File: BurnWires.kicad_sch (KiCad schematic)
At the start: 29 parts, among them Q13 IRLML2803, Q14 SiRA99DP, Q15 IRFTS9342PBF, Q17 IRFTS9342PBF, Q19 IRFTS9342PBF

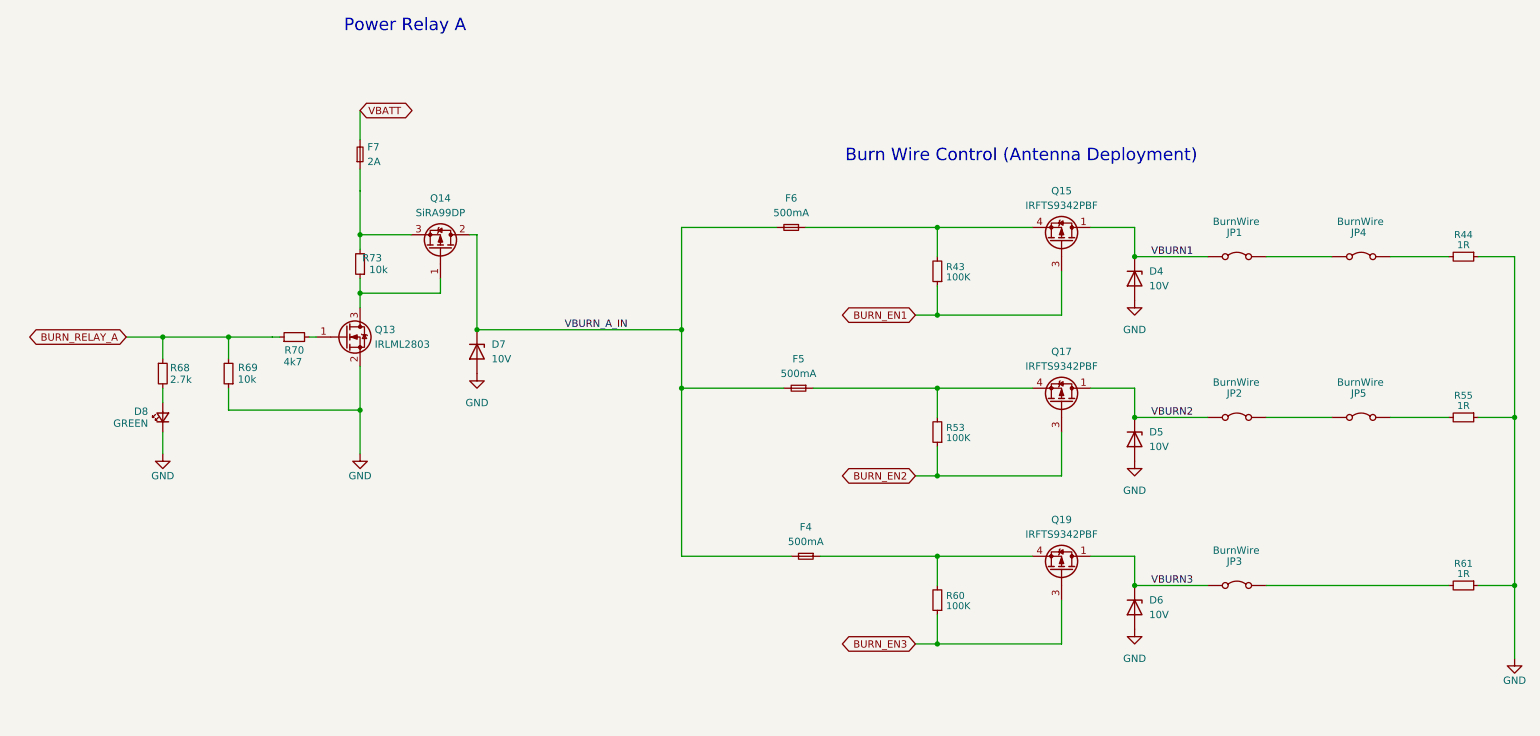
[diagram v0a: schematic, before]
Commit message: Updated burnwire footprint and fuse specs
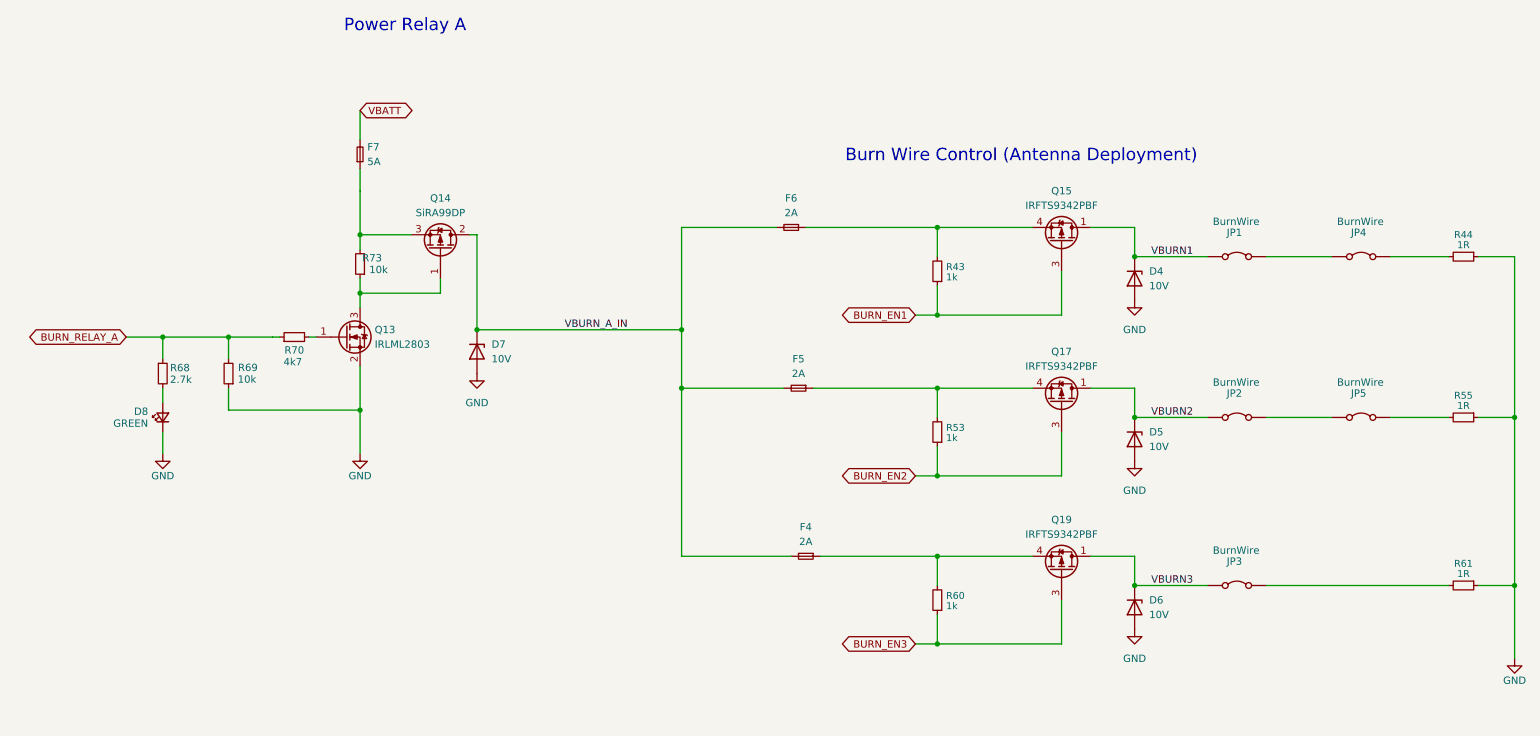
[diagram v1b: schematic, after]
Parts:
- F4, F5, F6: value 500mA -> 2A
- F7: value 2A -> 5A
- R43, R53, R60: value 100K -> 1k
- R44, R55, R61: footprint Resistor_SMD:R_1206_3216Metric -> Resistor_SMD:R_2512_6332Metric
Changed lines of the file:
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@@
 			)
 		)
-		(property "Value" "100K"
+		(property "Value" "1k"
 			(at 179.324 102.616 0)
 			(effects
@@
 			)
 		)
-		(property "Footprint" "Resistor_SMD:R_1206_3216Metric"
+		(property "Footprint" "Resistor_SMD:R_2512_6332Metric"
 			(at 269.24 71.12 0)
 			(effects
@@
 			)
 		)
-		(property "Value" "500mA"
+		(property "Value" "2A"
 			(at 153.67 91.44 0)
 			(effects
@@
 			)
 		)
-		(property "Footprint" "Resistor_SMD:R_1206_3216Metric"
+		(property "Footprint" "Resistor_SMD:R_2512_6332Metric"
 			(at 269.24 128.27 0)
 			(effects
@@
 			)
 		)
-		(property "Value" "2A"
+		(property "Value" "5A"
 			(at 78.74 54.6099 90)
 			(effects
@@
 			)
 		)
-		(property "Value" "100K"
+		(property "Value" "1k"
 			(at 179.324 74.676 0)
 			(effects
@@
 			)
 		)
-		(property "Value" "500mA"
+		(property "Value" "2A"
 			(at 154.94 120.65 0)
 			(effects
@@
 			)
 		)
-		(property "Value" "100K"
+		(property "Value" "1k"
 			(at 179.324 131.826 0)
 			(effects
@@
 			)
 		)
-		(property "Value" "500mA"
+		(property "Value" "2A"
 			(at 152.4 63.5 0)
 			(effects
@@
 			)
 		)
-		(property "Footprint" "Resistor_SMD:R_1206_3216Metric"
+		(property "Footprint" "Resistor_SMD:R_2512_6332Metric"
 			(at 269.24 99.06 0)
 			(effects

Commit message: push
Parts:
- removed D7: 10V, Diode_SMD:Nexperia_DSN1608-2_1.6x0.8mm, symbol Diode:PTVS10VZ1USK
- removed D8: GREEN, LED_SMD:LED_0603_1608Metric, symbol Device:LED_Small
- removed Q14: SiRA99DP, Argus-Miscellaneous:PowerPAK SO-8, symbol Argus-IC:Q_PMOS_GDS
- removed R73: 10k, Resistor_SMD:R_0603_1608Metric, symbol Device:R_Small
- added D1: 10V, Diode_SMD:Nexperia_DSN1608-2_1.6x0.8mm, symbol Diode:PTVS10VZ1USK
- added D7: GREEN, LED_SMD:LED_0603_1608Metric, symbol Device:LED_Small
- added F8: 1A, Fuse:Fuse_0603_1608Metric, symbol Device:Fuse_Small
- added K1: G6B-1114P-US DC6, Argus-Miscellaneous:RELAY_G6B-1114P-US_OMR, symbol Argus-Miscellaneous:G6B-1114P-US_DC6
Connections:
- net GND: now also D1.2 (A), D7.1 (K)
- net VBATT: now also F8.2
- net at Q13.3 (D): now also K1.1
- net at F7.1: now also K1.3
- net at R68.2: now also D7.2 (A)
- net VBURN_A_IN: no longer names the net of F4.2, F5.2, F6.2
- net VBURN_A_IN: now also D1.1 (K), K1.4
- new net: F8.1, K1.6

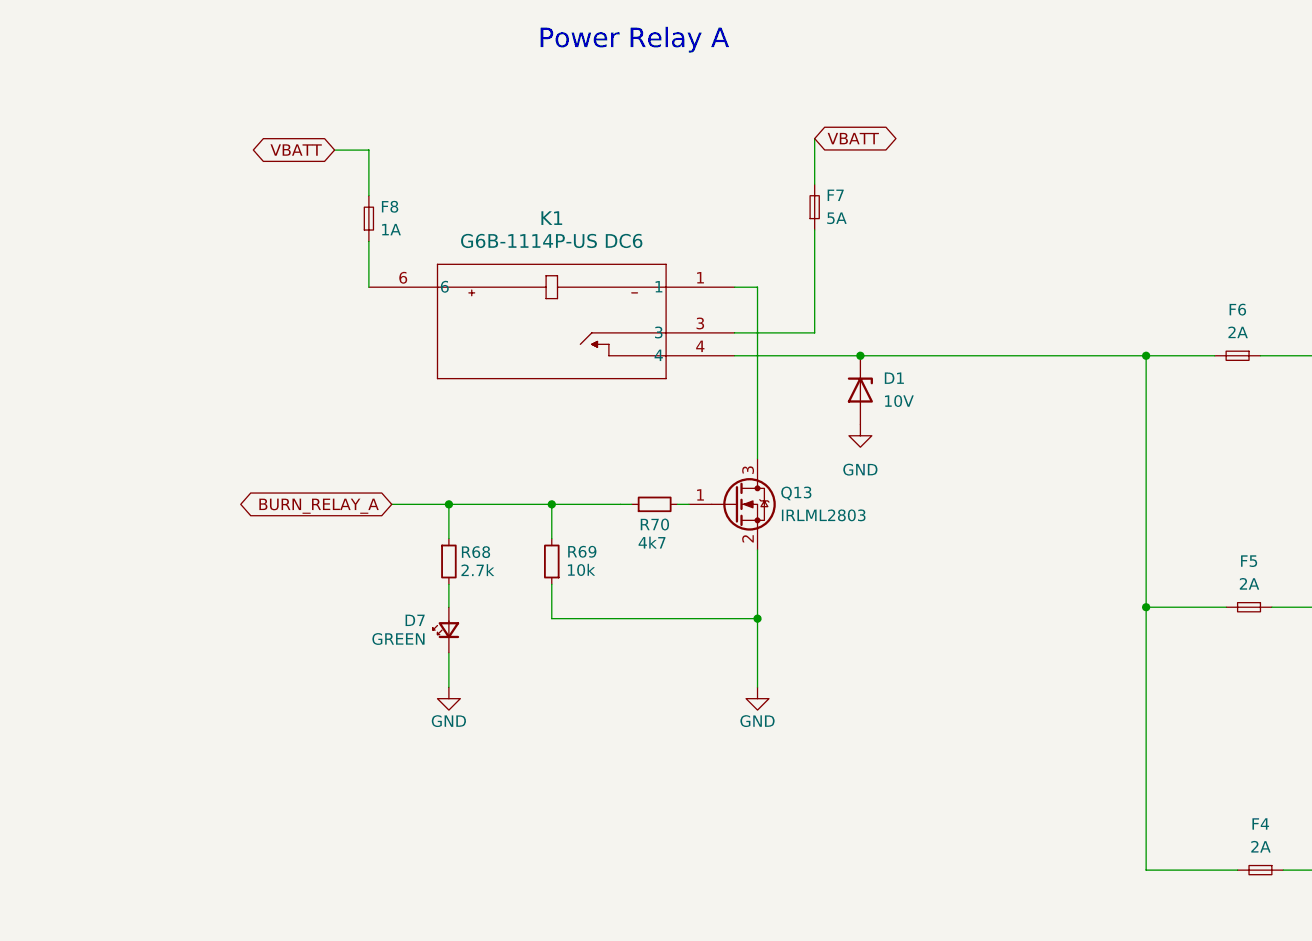
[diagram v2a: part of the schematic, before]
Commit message: updated relay with old relay
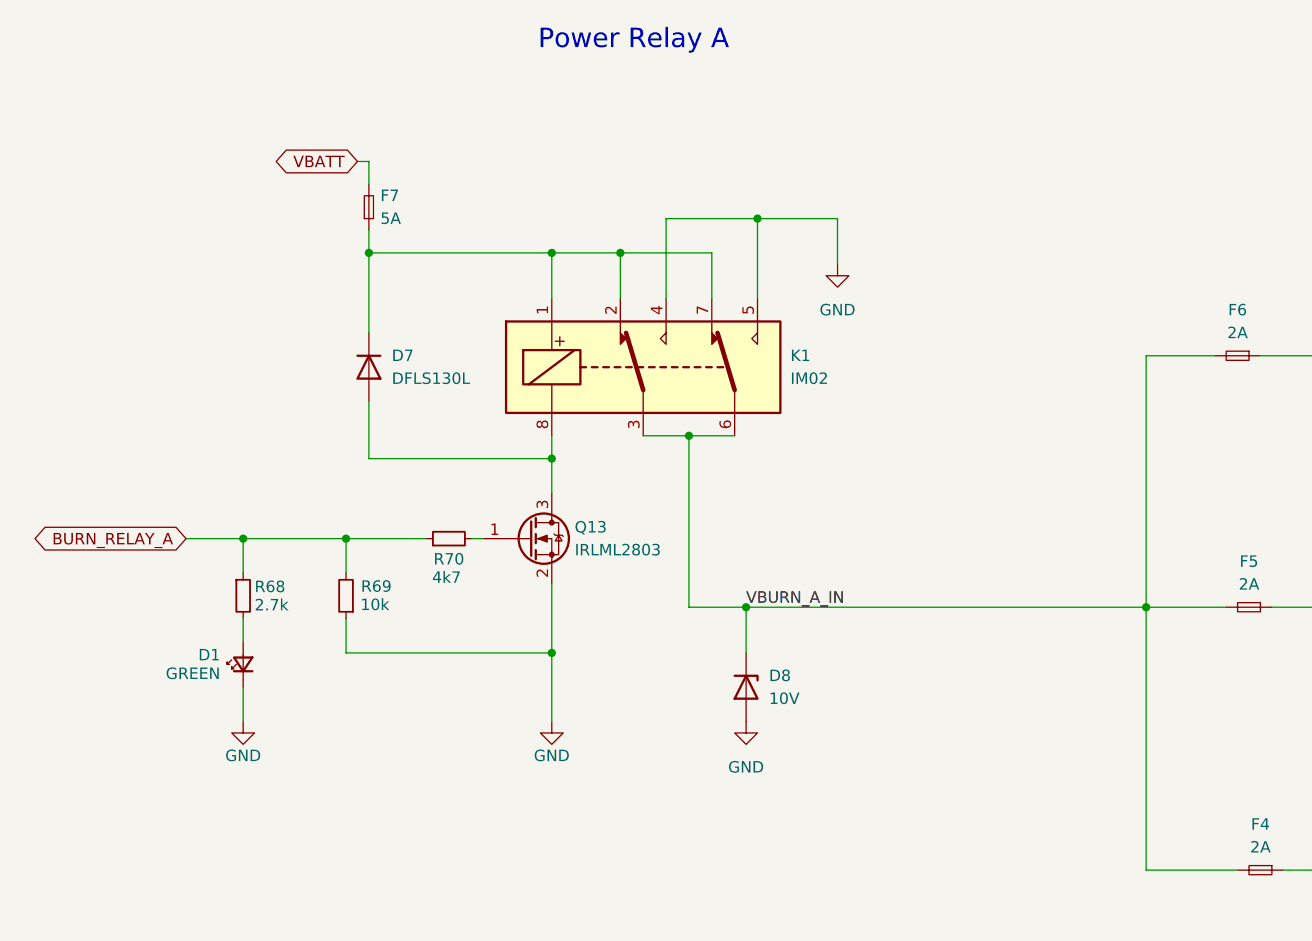
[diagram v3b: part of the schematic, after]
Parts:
- removed D1: 10V, Diode_SMD:Nexperia_DSN1608-2_1.6x0.8mm, symbol Diode:PTVS10VZ1USK
- removed D7: GREEN, LED_SMD:LED_0603_1608Metric, symbol Device:LED_Small
- removed F8: 1A, Fuse:Fuse_0603_1608Metric, symbol Device:Fuse_Small
- removed K1: G6B-1114P-US DC6, Argus-Miscellaneous:RELAY_G6B-1114P-US_OMR, symbol Argus-Miscellaneous:G6B-1114P-US_DC6
- added D1: GREEN, LED_SMD:LED_0603_1608Metric, symbol Device:LED_Small
- added D7: DFLS130L, Diode_SMD:D_PowerDI-123, symbol Device:D
- added D8: 10V, Diode_SMD:Nexperia_DSN1608-2_1.6x0.8mm, symbol Diode:PTVS10VZ1USK
- added K1: IM02, Argus-Miscellaneous:RELAY8_SMTGUL_TEC, symbol Relay:IM02
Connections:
- net GND: now also D1.1 (K), D8.2 (A), K1.4, K1.5
- net at Q13.3 (D): now also D7.2 (A), K1.8
- net at F7.1: now also D7.1 (K), K1.1, K1.2, K1.7
- net VBURN_A_IN: now reaches F4.2, F5.2, F6.2
- net VBURN_A_IN: now also D8.1 (K), K1.3, K1.6
- net at R68.2: now also D1.2 (A)

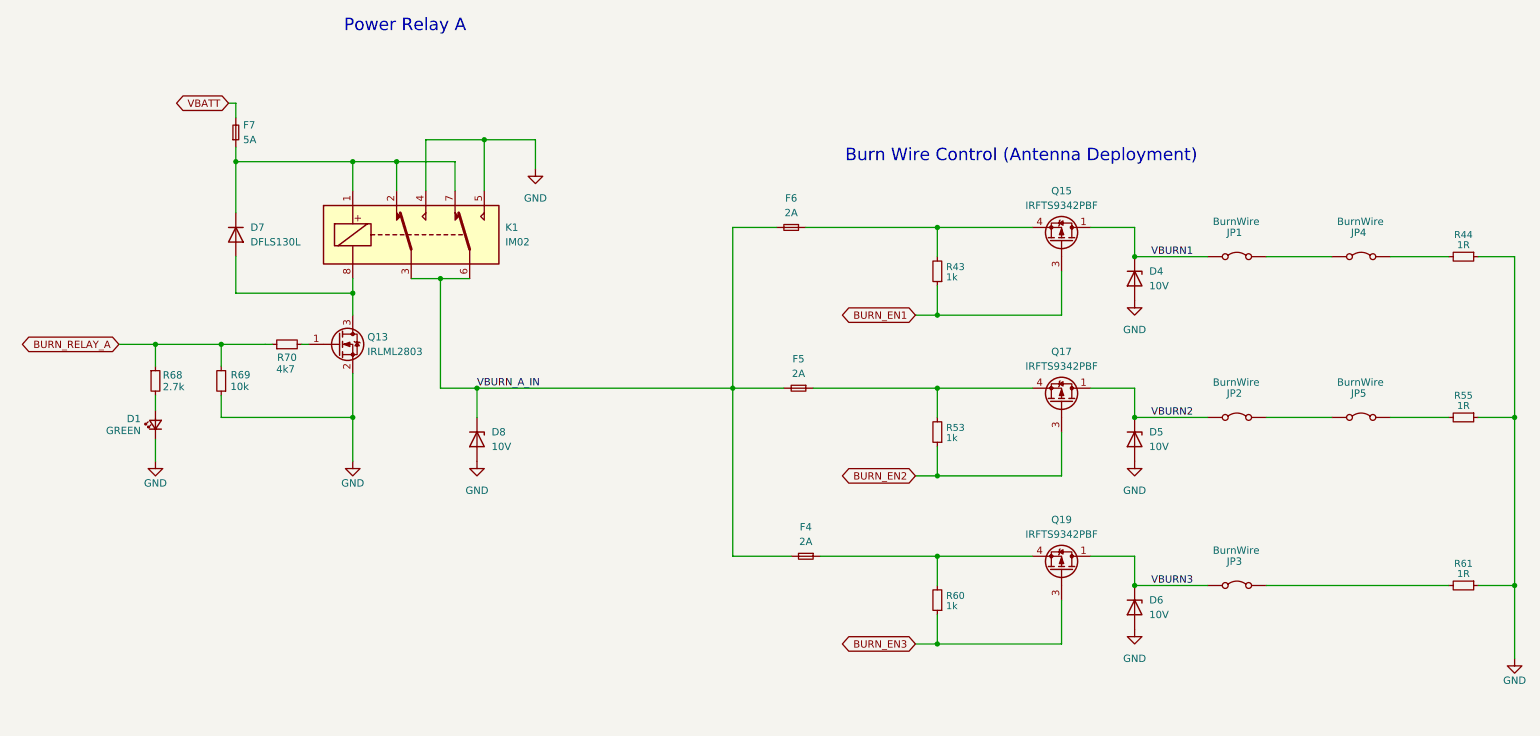
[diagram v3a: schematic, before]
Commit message: Updated burnwire circuitry and layout
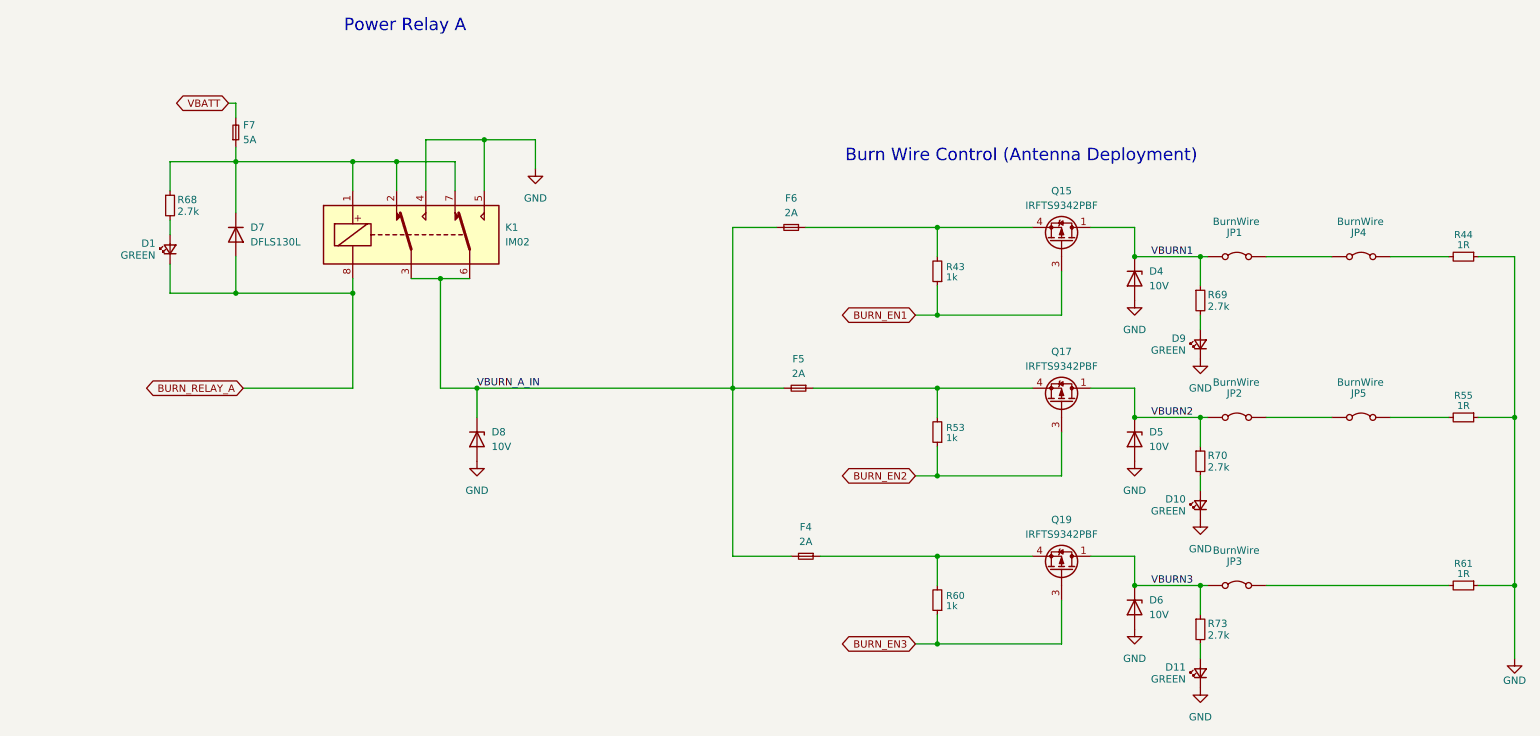
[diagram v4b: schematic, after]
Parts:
- removed Q13: IRLML2803, Package_TO_SOT_SMD:SOT-23, symbol Argus-IC:IRLML2803
- added D10, D11, D9: GREEN, LED_SMD:LED_0603_1608Metric, symbol Device:LED_Small
- added R73: 2.7k, Resistor_SMD:R_0603_1608Metric, symbol Device:R_Small
- R69: value 10k -> 2.7k; DPN 311-10.0KHRCT-ND -> A129693CT-ND; MFR Yageo -> TE; MPN RC0603FR-0710KL -> CRGCQ0603F2K7
- R70: value 4k7 -> 2.7k; DIS (none) -> Digi-Key; DPN (none) -> A129693CT-ND; MFR (none) -> TE; MPN (none) -> CRGCQ0603F2K7
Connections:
- net BURN_RELAY_A: now also D1.1 (K), D7.2 (A), K1.8; no longer R68.1, R69.2, R70.1
- net GND: now also D10.1 (K), D11.1 (K), D9.1 (K); no longer D1.1 (K), R69.1
- net VBURN1: now also R69.1
- net VBURN2: now also R70.1
- net VBURN3: now also R73.1
- net at R70.2: now also D10.2 (A)
- net at D7.1 (K), F7.1, K1.1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: now also R68.1
- new net: D9.2 (A), R69.2
- new net: D11.2 (A), R73.2

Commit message: Stash
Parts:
- removed D4, D5, D6, D8: 10V, Diode_SMD:Nexperia_DSN1608-2_1.6x0.8mm, symbol Diode:PTVS10VZ1USK
- removed F7: 5A, Fuse:Fuse_0603_1608Metric, symbol Device:Fuse_Small
- removed K1: IM02, Argus-Miscellaneous:RELAY8_SMTGUL_TEC, symbol Relay:IM02
- removed R53, R60: 1k, Resistor_SMD:R_0603_1608Metric, symbol Device:R_Small
- removed R68: 2.7k, Resistor_SMD:R_0603_1608Metric, symbol Device:R_Small
- added Q10, Q6, Q8: IRLML2803, Package_TO_SOT_SMD:SOT-23, symbol Argus-IC:IRLML2803
- added Q5: MMBT2222AT, Package_TO_SOT_SMD:SOT-23, symbol mainboard:MMBT2222AT
- added R15, R18: TBD, Resistor_SMD:R_0603_1608Metric, symbol Device:R_Small
- added R16, R19, R25, R31: 0R, Resistor_SMD:R_0603_1608Metric, symbol Device:R_Small
- added R17, R21, R27, R33: 10k, Resistor_SMD:R_0603_1608Metric, symbol Device:R_Small
- added R20, R26, R32: 4k7, Resistor_SMD:R_0603_1608Metric, symbol Device:R_Small
- added R28, R34: 1k, Resistor_SMD:R_0603_1608Metric, symbol Device:R_Small
- added R78: 2k7, Resistor_SMD:R_0603_1608Metric, symbol Device:R_Small
- added U2: PE014006, Argus-Miscellaneous:RELAY_PE014006, symbol mainboard:PE014005
- D1: renamed from D7; value DFLS130L -> DFLS130LQ-7
- F2: renamed from F6; value 2A -> 5A
- F3: renamed from F5; value 2A -> 5A
- F4: value 2A -> 5A
- R23: renamed from R69; value 2.7k -> 2k7
- R29: renamed from R70; value 2.7k -> 2k7
- R35: renamed from R73; value 2.7k -> 2k7
- renumbered D1 to D2, D9 to D3, D10 to D4, D11 to D5, JP4 to JP2, JP2 to JP3, JP5 to JP4, JP3 to JP5, Q19 to Q11, Q15 to Q7, Q17 to Q9, R43 to R22, R44 to R24, R55 to R30, R61 to R36
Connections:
- net BURN_EN1: now also R19.2, R20.2, R21.1; no longer Q7.3 (G), R22.1
- net BURN_EN2: now also R25.2, R26.2, R27.1; no longer Q9.3 (G)
- net BURN_EN3: now also R31.2, R32.2, R33.1; no longer Q11.3 (G)
- net BURN_RELAY_A: now also R15.1; no longer D1.2 (A), D2.1 (K)
- net GND: now also D2.1 (K), Q10.2 (S), Q6.2 (S), Q8.2 (S), R18.2, R21.2, R27.2, R33.2, U2.12
- net VBATT: now also D1.1 (K), U2.14, U2.A1
- net VBURN_A_IN: now also R78.1, U2.11
- net at F3.1, Q9.4 (S): now also R28.2
- net at F4.1, Q11.4 (S): now also R34.2
- net at D2.2 (A): now also R78.2
- new net: D1.2 (A), Q5.3 (C), R16.2, U2.A2
- new net: Q5.1 (B), R15.2, R16.1, R17.1
- new net: Q6.3 (D), Q7.3 (G), R19.1, R22.1
- new net: Q10.3 (D), Q11.3 (G), R31.1, R34.1
- new net: Q8.1 (G), R26.1
- new net: Q8.3 (D), Q9.3 (G), R25.1, R28.1
- new net: Q5.2 (E), R17.2, R18.1
- new net: Q6.1 (G), R20.1
- new net: Q10.1 (G), R32.1
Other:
- company: (none) -> N. Khera
- title: (none) -> Argus -Z Panel
- moved on the sheet: D1, D2, D3, D4, D5, F2, F3, F4, JP1, JP2, JP3, JP4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

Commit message: resistor values
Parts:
- R15: value TBD -> 330R
- R18: value TBD -> 0R
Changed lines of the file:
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@@
 			)
 		)
-		(property "Value" "TBD"
+		(property "Value" "330R"
 			(at 43.18 113.538 90)
 			(effects
@@
 			)
 		)
-		(property "Value" "TBD"
+		(property "Value" "0R"
 			(at 62.23 131.826 0)
 			(effects
